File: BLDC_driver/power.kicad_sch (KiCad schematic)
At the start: 0 parts

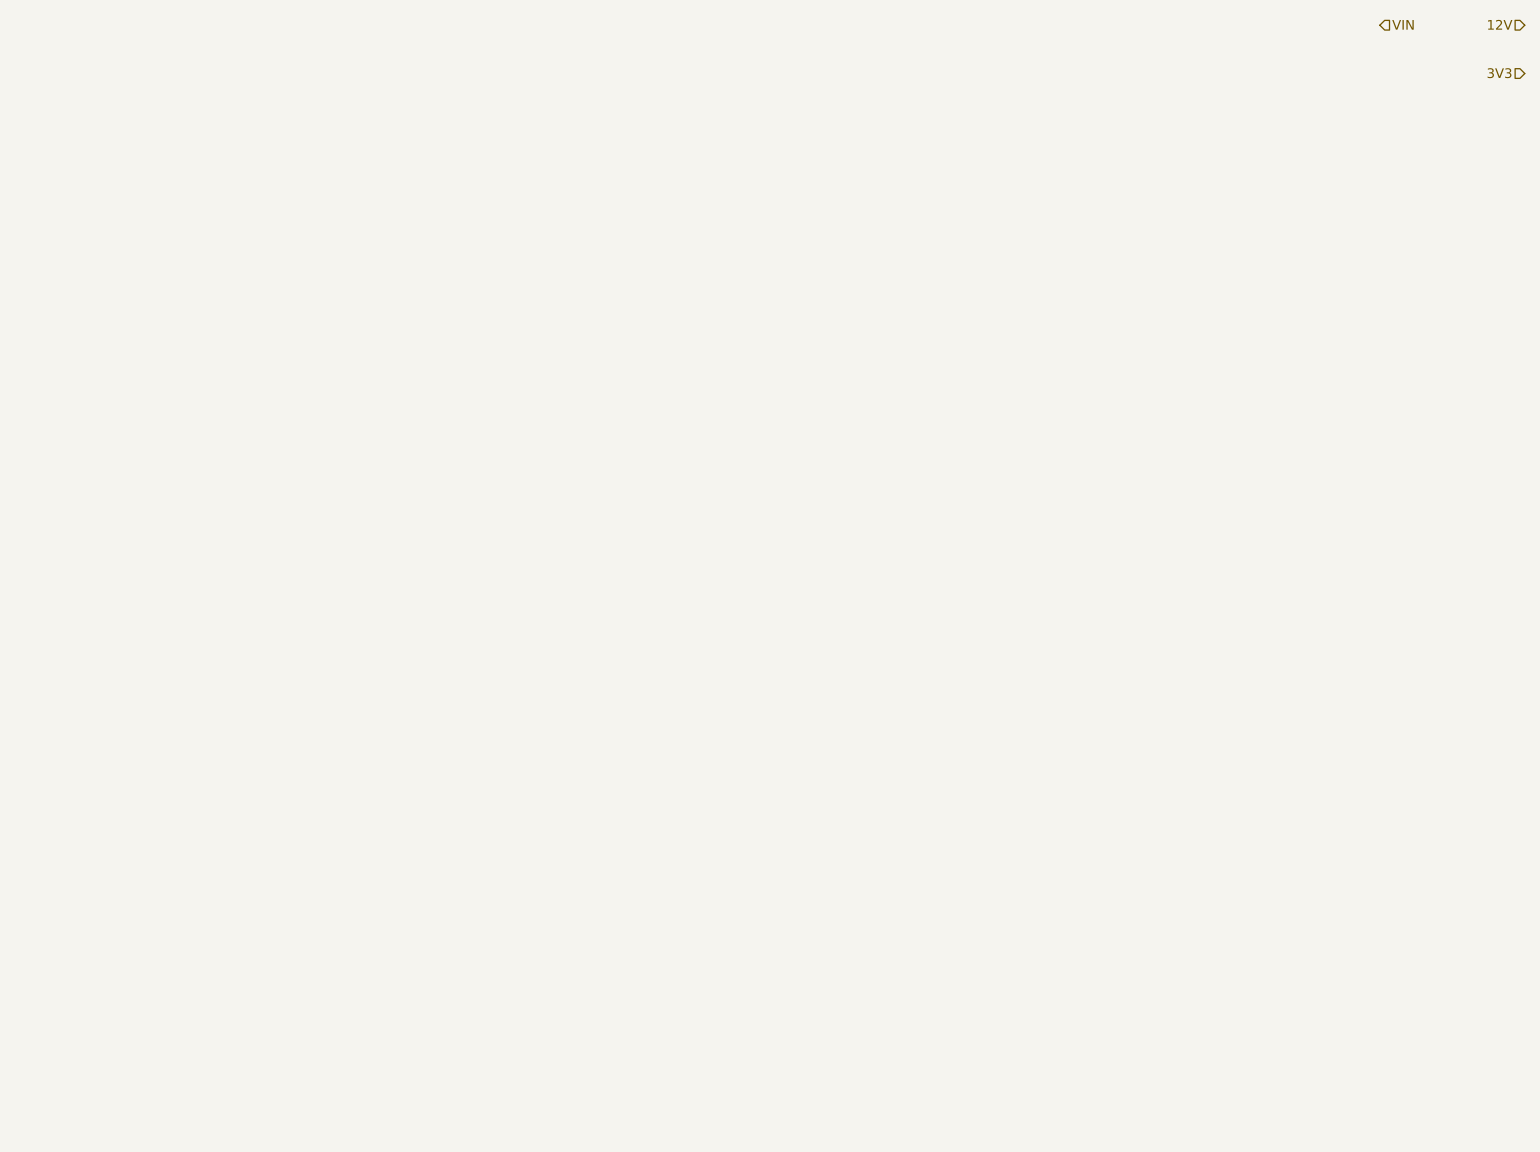
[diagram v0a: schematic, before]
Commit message: Started on power conversion section
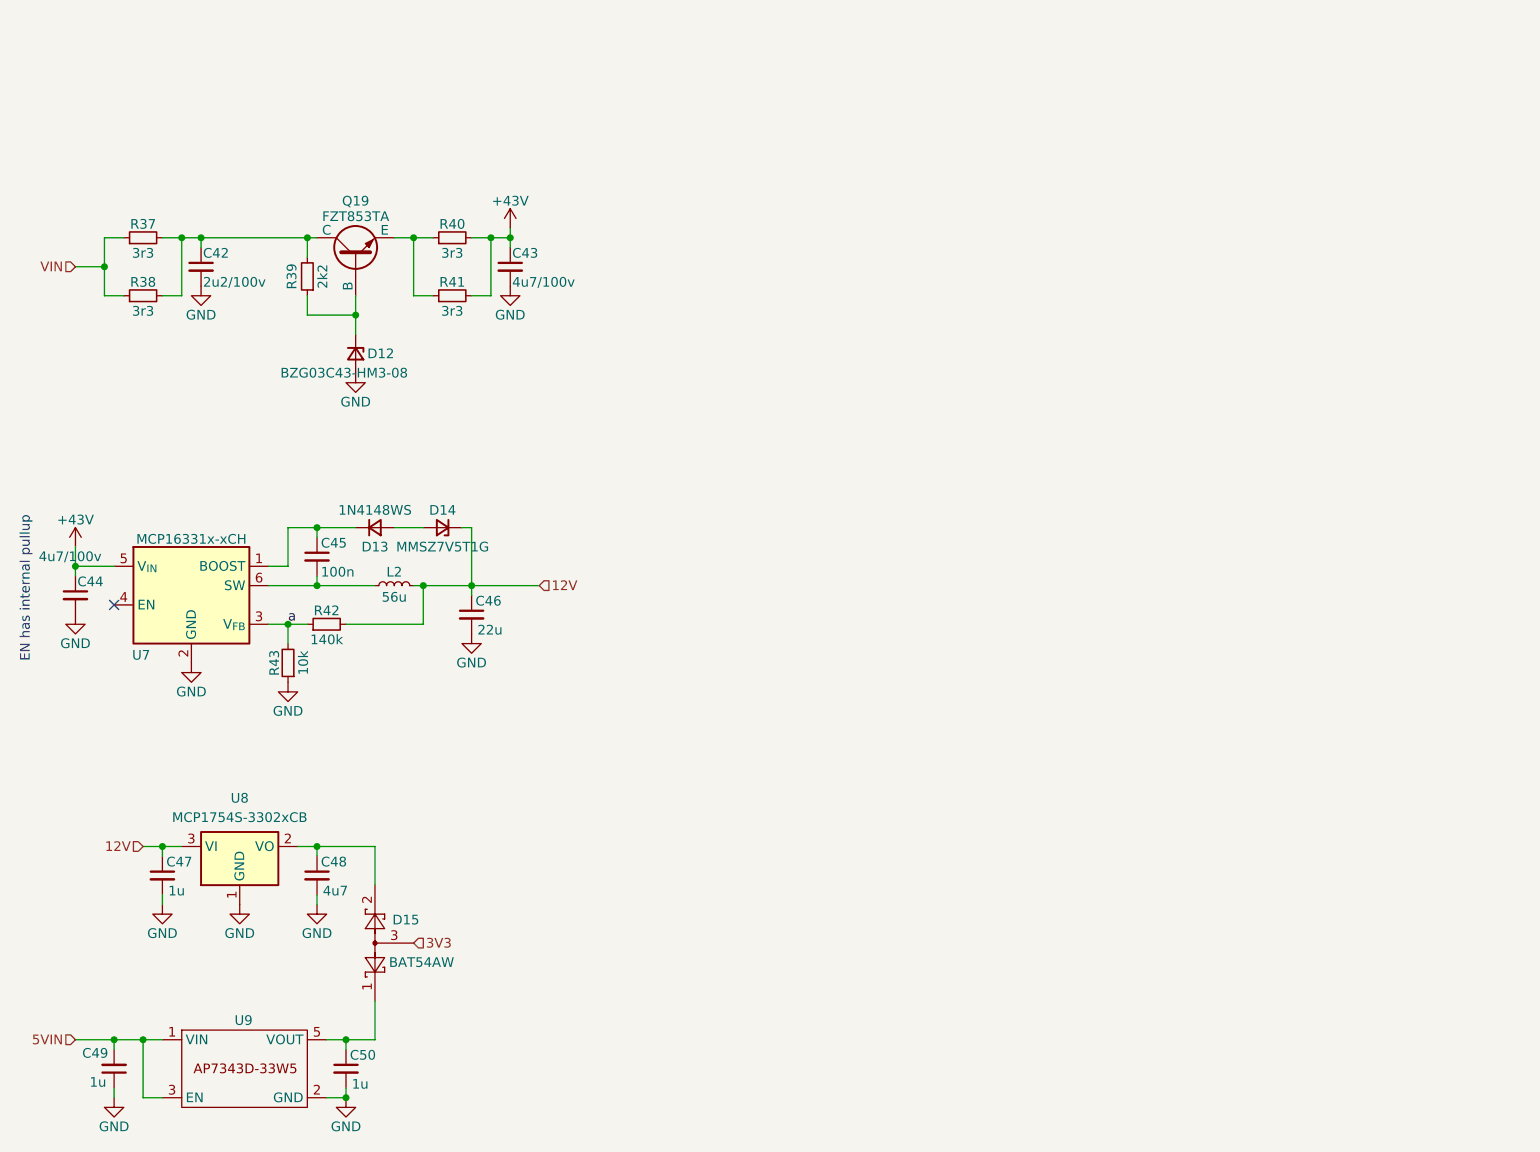
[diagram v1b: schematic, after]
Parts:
- added C42: 2u2/100v, Capacitor_SMD:C_1210_3225Metric, symbol Device:C_Small
- added C43, C44: 4u7/100v, Capacitor_SMD:C_1210_3225Metric, symbol Device:C_Small
- added C45: 100n, Capacitor_SMD:C_0603_1608Metric, symbol Device:C_Small
- added C46: 22u, Capacitor_SMD:C_0603_1608Metric, symbol Device:C_Small
- added C47, C49, C50: 1u, Capacitor_SMD:C_0603_1608Metric, symbol Device:C_Small
- added C48: 4u7, Capacitor_SMD:C_0603_1608Metric, symbol Device:C_Small
- added D12: BZG03C43-HM3-08, Diode_SMD:D_SMB, symbol Device:D_Zener_Small
- added D13: 1N4148WS, Diode_SMD:D_SOD-323_HandSoldering, symbol Device:D_Small
- added D14: MMSZ7V5T1G, Diode_SMD:D_SOD-123, symbol Device:D_Zener_Small
- added D15: BAT54AW, Package_TO_SOT_SMD:SOT-323_SC-70, symbol Diode:BAT54AW
- added L2: 56u, Inductor_SMD:L_7.3x7.3_H4.5, symbol Device:L_Small
- added Q19: FZT853TA, Package_TO_SOT_SMD:SOT-223-3_TabPin2, symbol Simulation_SPICE:NPN
- added R37, R38, R40, R41: 3r3, Resistor_SMD:R_1206_3216Metric, symbol Device:R_Small
- added R39: 2k2, Resistor_SMD:R_1206_3216Metric, symbol Device:R_Small
- added R42: 140k, Resistor_SMD:R_0805_2012Metric, symbol Device:R_Small
- added R43: 10k, Resistor_SMD:R_0805_2012Metric, symbol Device:R_Small
- added U7: MCP16331x-xCH, Package_TO_SOT_SMD:SOT-23-6, symbol Regulator_Switching:MCP16331x-xCH
- added U8: MCP1754S-3302xCB, Package_TO_SOT_SMD:SOT-23, symbol Regulator_Linear:MCP1754S-3302xCB
- added U9: ~, Custom:SOT-25, symbol Marijn:AP7343D-33W5
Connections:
- net 12V: now also C46.1, C47.1, D14.1 (K), L2.2, R42.2, U8.3 (VI)
- net 3V3: now also D15.3
- net VIN: now also R37.1, R38.1
- new net: C42.1, Q19.1 (C), R37.2, R38.2, R39.2
- new net: Q19.3 (E), R40.1, R41.1
- new net: D13.2 (A), D14.2 (A)
- new net: C48.1, D15.2, U8.2 (VO)
- new net: D12.1 (K), Q19.2 (B), R39.1
- new net: C50.1, D15.1, U9.5 (VOUT)
- new net: C45.1, D13.1 (K), U7.1 (BOOST)
- new net: C45.2, L2.1, U7.6 (SW)
- new net +43V: C43.1, C44.1, R40.2, R41.2, U7.5 (V_{IN})
- new net 5VIN: C49.2, U9.1 (VIN), U9.3 (EN)
- new net GND: C42.2, C43.2, C44.2, C46.2, C47.2, C48.2, C49.1, C50.2, D12.2 (A), R43.1, U7.2 (GND), U8.1 (GND), U9.2 (GND)
- new net a: R42.1, R43.2, U7.3 (V_{FB})
- no-connect marks 0 -> 1
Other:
- note added: "EN has internal pullup"

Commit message: Power converter layout
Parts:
- removed D15: BAT54AW, Package_TO_SOT_SMD:SOT-323_SC-70, symbol Diode:BAT54AW
- removed U9: ~, Custom:SOT-25, symbol Marijn:AP7343D-33W5
- added D15: BAT54C, Package_TO_SOT_SMD:SOT-23, symbol Diode:BAT54C
- added U9: AP7343, Marijn_KiCad:SOT-25, symbol Marijn:AP7343
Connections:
- net 3V3: now also D15.3
- net 5VIN: now also U9.1 (VIN), U9.3 (EN)
- net GND: now also U9.2 (GND)
- net at C48.1, U8.2 (VO): now also D15.2
- net at C50.1: now also D15.1, U9.5 (VOUT)
- net a: no longer names the net of R42.1, R43.2, U7.3 (V_{FB})
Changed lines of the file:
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@@
-		)
-	)
-	(label "a"
-		(at 91.44 110.49 0)
-		(fields_autoplaced yes)
-		(effects
-			(font
-				(size 1.27 1.27)
-			)
-			(justify left bottom)
 		)
 	)
@@
 	)
 	(symbol
-		(lib_id "Diode:BAT54AW")
-		(at 102.87 152.4 90)
-		(unit 1)
-		(exclude_from_sim no)
-		(in_bom yes)
-		(on_board yes)
-		(dnp no)
-		(property "Reference" "D15"
-			(at 108.712 149.352 90)
-			(effects
-				(font
-					(size 1.27 1.27)
-				)
-				(justify left)
-			)
-		)
-		(property "Value" "BAT54AW"
-			(at 113.284 154.94 90)
-			(effects
-				(font
-					(size 1.27 1.27)
-				)
-				(justify left)
-			)
-		)
-		(property "Footprint" "Package_TO_SOT_SMD:SOT-323_SC-70"
-			(at 99.695 150.495 0)
-			(effects
-				(font
-					(size 1.27 1.27)
-				)
-				(justify left)
-				(hide yes)
-			)
-		)
-		(property "Datasheet" "https://assets.nexperia.com/documents/data-sheet/BAT54W_SER.pdf"
-			(at 102.87 155.448 0)
-			(effects
-				(font
-					(size 1.27 1.27)
-				)
-				(hide yes)
-			)
-		)
-		(property "Description" "Dual schottky barrier diode, common anode, SOT-323"
-			(at 102.87 152.4 0)
+		(lib_id "Marijn:AP7343")
+		(at 92.71 162.56 0)
+		(unit 1)
+		(exclude_from_sim no)
+		(in_bom yes)
+		(on_board yes)
+		(dnp no)
+		(property "Reference" "U9"
+			(at 92.71 162.814 0)
+			(effects
+				(font
+					(size 1.27 1.27)
+				)
+			)
+		)
+		(property "Value" "AP7343"
+			(at 85.725 162.56 0)
+			(effects
+				(font
+					(size 1.27 1.27)
+				)
+			)
+		)
+		(property "Footprint" "Marijn_KiCad:SOT-25"
+			(at 85.598 177.546 0)
+			(effects
+				(font
+					(size 1.27 1.27)
+				)
+				(hide yes)
+			)
+		)
+		(property "Datasheet" "https://stm32-base.org/assets/pdf/regulators/AP7343.pdf"
+			(at 85.598 175.26 0)
+			(effects
+				(font
+					(size 1.27 1.27)
+				)
+				(hide yes)
+			)
+		)
+		(property "Description" "5v -> 3v3"
+			(at 82.804 162.56 0)
 			(effects
 				(font
@@
 		(pin "3"
 		)
-		(pin "1"
-		)
 		(pin "2"
 		)
-		(instances
-			(project ""
-				(path "/6f399879-dc45-4210-87b6-ea005f89c132/cf979161-f881-4975-b113-b0ad6afb809e"
-					(reference "D15")
+		(pin "1"
+		)
+		(pin "5"
+		)
+		(instances
+			(project "BLDC_driver"
+				(path "/6f399879-dc45-4210-87b6-ea005f89c132/cf979161-f881-4975-b113-b0ad6afb809e"
+					(reference "U9")
 					(unit 1)
 				)
@@
 	)
 	(symbol
-		(lib_id "Marijn:AP7343D-33W5")
-		(at 92.71 162.56 0)
-		(unit 1)
-		(exclude_from_sim no)
-		(in_bom yes)
-		(on_board yes)
-		(dnp no)
-		(property "Reference" "U9"
-			(at 85.598 162.56 0)
-			(effects
-				(font
-					(size 1.27 1.27)
-				)
-			)
-		)
-		(property "Value" "~"
-			(at 85.725 162.56 0)
-			(effects
-				(font
-					(size 1.27 1.27)
-				)
-			)
-		)
-		(property "Footprint" "Custom:SOT-25"
-			(at 85.598 177.546 0)
-			(effects
-				(font
-					(size 1.27 1.27)
-				)
-				(hide yes)
-			)
-		)
-		(property "Datasheet" "https://stm32-base.org/assets/pdf/regulators/AP7343.pdf"
-			(at 85.598 175.26 0)
-			(effects
-				(font
-					(size 1.27 1.27)
-				)
-				(hide yes)
-			)
-		)
-		(property "Description" "5v -> 3v3"
-			(at 82.804 162.56 0)
-			(effects
-				(font
-					(size 1.27 1.27)
-				)
-				(hide yes)
-			)
-		)
-		(pin "5"
-		)
-		(pin "3"
-		)
-		(pin "1"
-		)
-		(pin "2"
-		)
-		(instances
-			(project ""
-				(path "/6f399879-dc45-4210-87b6-ea005f89c132/cf979161-f881-4975-b113-b0ad6afb809e"
-					(reference "U9")
-					(unit 1)
-				)
-			)
-		)
-	)
-	(symbol
 		(lib_id "power:GND")
 		(at 100.33 77.47 0)
@@
 					(unit 1)
 				)
+			)
+		)
+	)
+	(symbol
+		(lib_id "Diode:BAT54C")
+		(at 102.87 152.4 90)
+		(unit 1)
+		(exclude_from_sim no)
+		(in_bom yes)
+		(on_board yes)
+		(dnp no)
+		(property "Reference" "D15"
+			(at 111.506 150.368 90)
+			(effects
+				(font
+					(size 1.27 1.27)
+				)
+				(justify left)
+			)
+		)
+		(property "Value" "BAT54C"
+			(at 113.284 154.432 90)
+			(effects
+				(font
+					(size 1.27 1.27)
+				)
+				(justify left)
+			)
+		)
+		(property "Footprint" "Package_TO_SOT_SMD:SOT-23"
+			(at 99.695 150.495 0)
+			(effects
+				(font
+					(size 1.27 1.27)
+				)
+				(justify left)
+				(hide yes)
+			)
+		)
+		(property "Datasheet" "http://www.diodes.com/_files/datasheets/ds11005.pdf"
+			(at 102.87 154.432 0)
+			(effects
+				(font
+					(size 1.27 1.27)
+				)
+				(hide yes)
+			)
+		)
+		(property "Description" "dual schottky barrier diode, common cathode"
+			(at 102.87 152.4 0)
+			(effects
+				(font
+					(size 1.27 1.27)
+				)
+				(hide yes)
+			)
+		)
+		(pin "2"
+		)
+		(pin "1"
+		)
+		(pin "3"
+		)
+		(instances
+			(project "BLDC_driver"
+				(path "/6f399879-dc45-4210-87b6-ea005f89c132/cf979161-f881-4975-b113-b0ad6afb809e"
+					(reference "D15")
+					(unit 1)
+				)
